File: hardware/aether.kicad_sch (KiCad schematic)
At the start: 42 parts, among them Q1 S8050_C2146, U1 USBLC6-2SC6, U12 SI5448DU-T1-GE3, U14 SI5448DU-T1-GE3, U3 SI5448DU-T1-GE3, U7 SI5448DU-T1-GE3

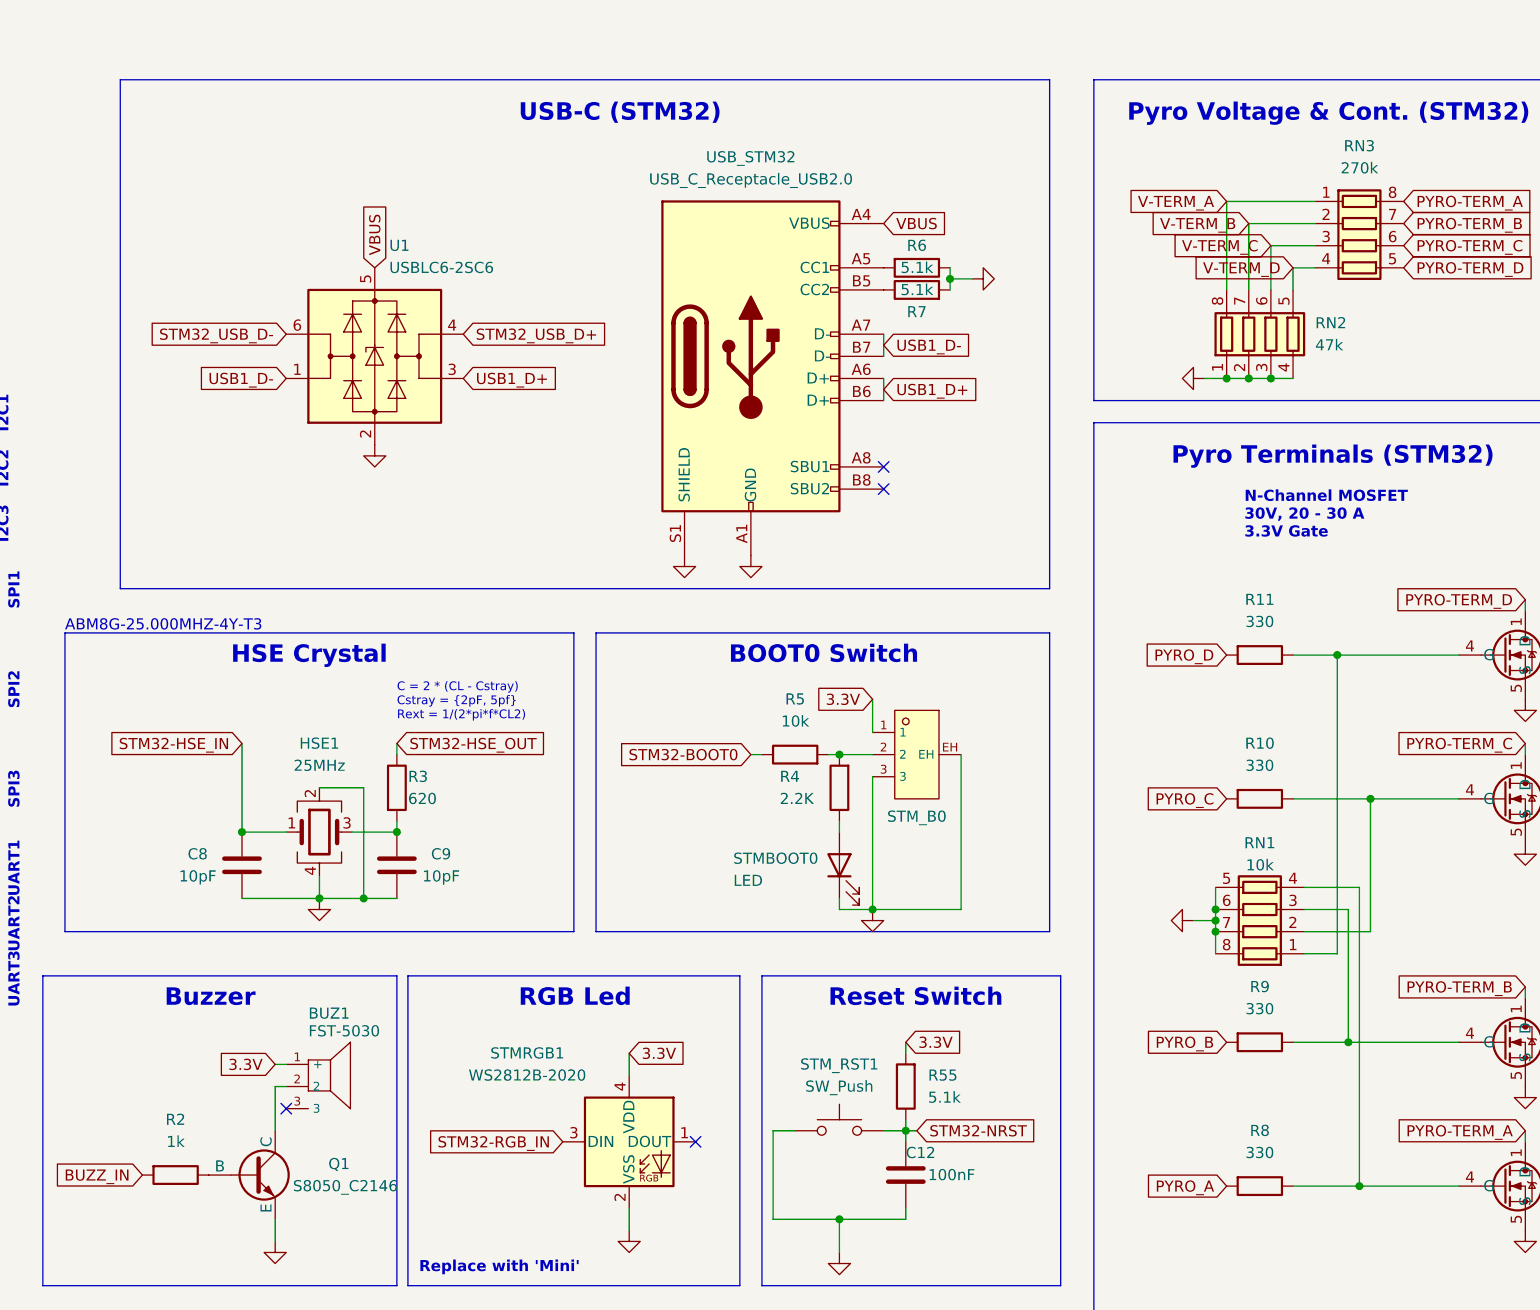
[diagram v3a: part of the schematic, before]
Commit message: Updated minimum via hole size to 0.3mm.
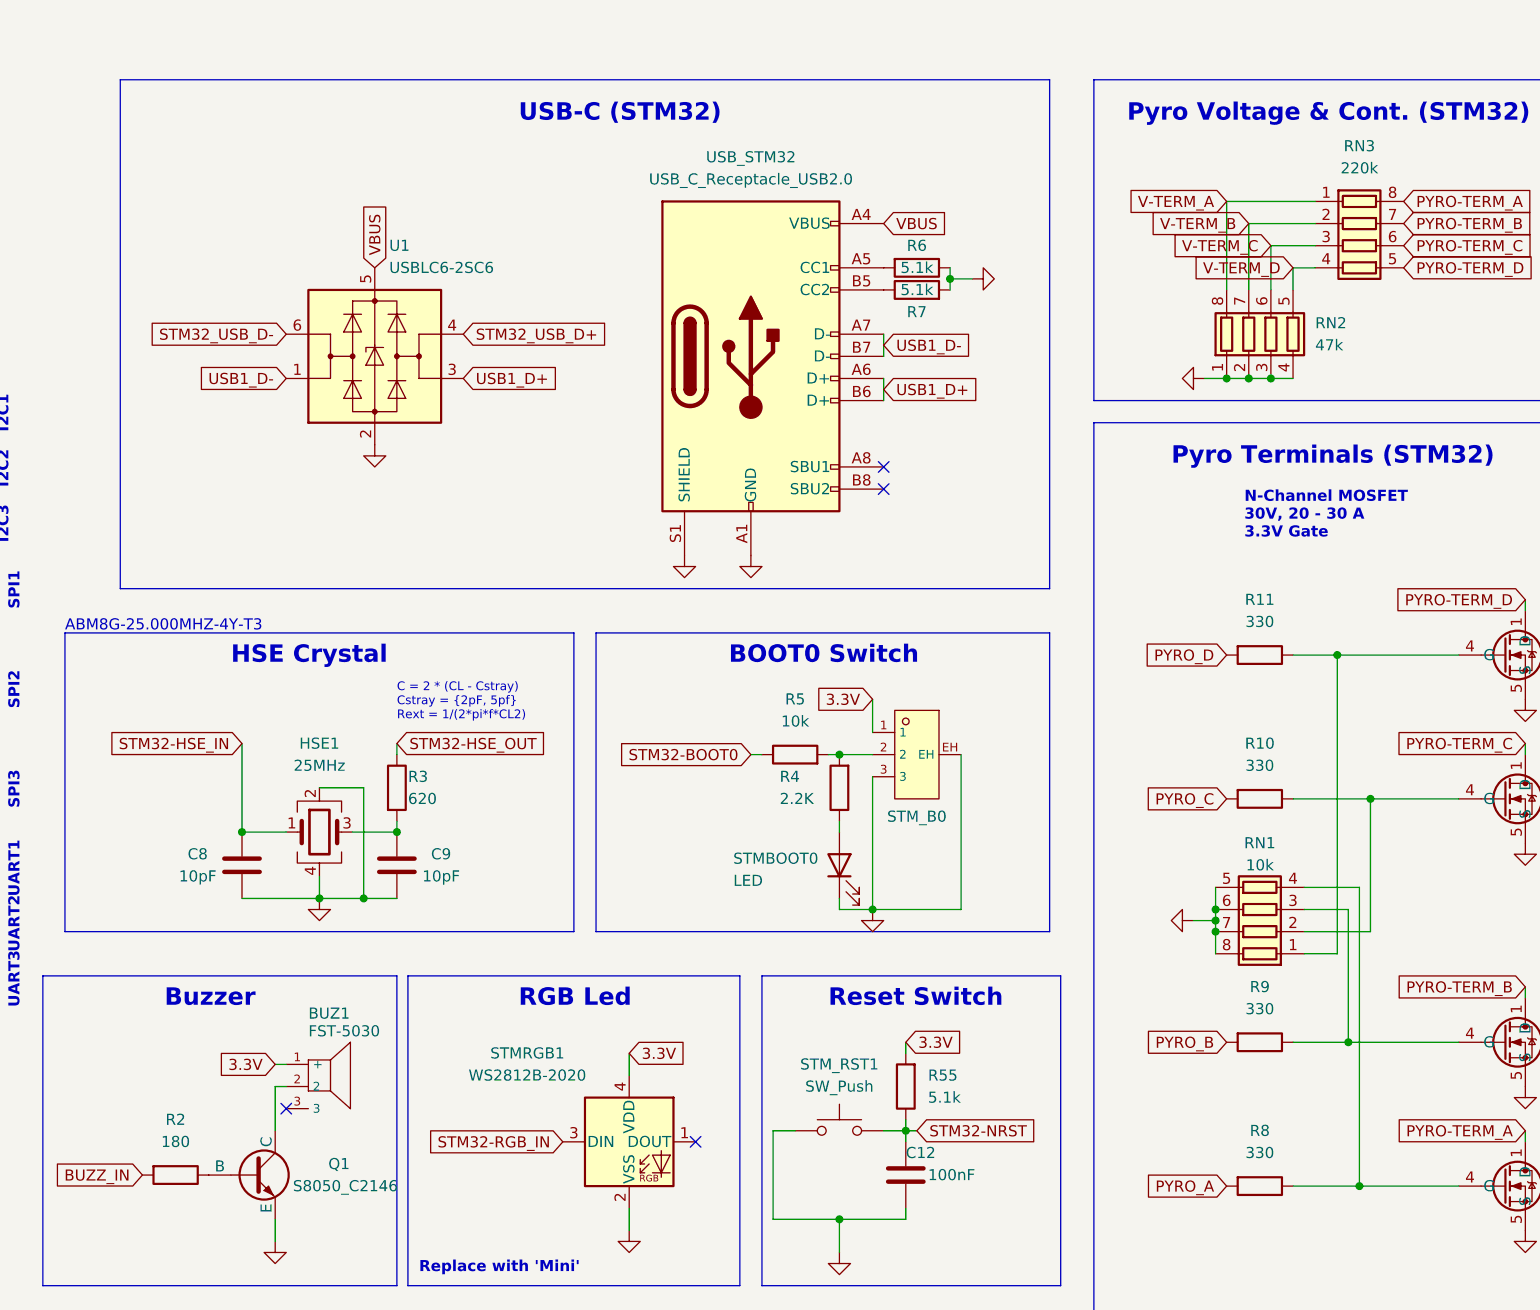
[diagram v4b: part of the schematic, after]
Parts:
- R2: value 1k -> 180
- RN3: value 270k -> 220k
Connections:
- net GND: now also Q1.2 (E); no longer Q1.3 (E)
- net at Q1.1 (B): now also R2.1; no longer BUZ1.2
- new net: BUZ1.2, Q1.3 (C)
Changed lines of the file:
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@@
 			)
 		)
-		(property "Value" "270k"
+		(property "Value" "220k"
 			(at 255.27 26.67 90)
 			(effects
@@
 			)
 		)
-		(property "Value" "1k"
+		(property "Value" "180"
 			(at 119.38 138.43 90)
 			(effects
